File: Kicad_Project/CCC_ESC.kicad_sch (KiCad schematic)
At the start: 218 parts, among them J1 Conn_01x07, J2 Conn_01x06, J3 Conn_01x06, J4 Conn_01x06, SW1 Conn_01x02, U1 NCP5183 / TF2190-TAH, U2 NCP5183 / TF2190-TAH, U3 NCP5183 / TF2190-TAH, U4 NCS20034DR2G, U5 STM32F401CCU6_Balckpill, U6 PQDE6W-Q110 / RD5-110S12W, U7 TO220_replacement_module

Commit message: initial layout approach
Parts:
- QA1, QA2, QA3, QA4, QA5, QA6: footprint CCC_ESC_Custom_parts:TO220_horizontal_smallgate -> Package_DFN_QFN:DFNW-8_L8.3-W8.4-P2.00-BL
- TpGS1, TpGS2, TpGS3, TpGS4, TpGS5, TpGS6: footprint TestPoint:TestPoint_THTPad_D2.0mm_Drill1.0mm -> TestPoint:TestPoint_THTPad_D1.5mm_Drill0.7mm
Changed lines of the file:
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@@
       (effects (font (size 1.27 1.27)) (justify left) hide)
     )
-    (property "Footprint" "CCC_ESC_Custom_parts:TO220_horizontal_smallgate" (at 504.19 55.88 0)
+    (property "Footprint" "Package_DFN_QFN:DFNW-8_L8.3-W8.4-P2.00-BL" (at 504.19 55.88 0)
       (effects (font (size 1.27 1.27)) hide)
     )
@@
       (effects (font (size 1.27 1.27)) (justify left) hide)
     )
-    (property "Footprint" "CCC_ESC_Custom_parts:TO220_horizontal_smallgate" (at 474.98 55.88 0)
+    (property "Footprint" "Package_DFN_QFN:DFNW-8_L8.3-W8.4-P2.00-BL" (at 474.98 55.88 0)
       (effects (font (size 1.27 1.27)) hide)
     )
@@
       (effects (font (size 1.27 1.27)) (justify left) hide)
     )
-    (property "Footprint" "CCC_ESC_Custom_parts:TO220_horizontal_smallgate" (at 474.98 76.2 0)
+    (property "Footprint" "Package_DFN_QFN:DFNW-8_L8.3-W8.4-P2.00-BL" (at 474.98 76.2 0)
       (effects (font (size 1.27 1.27)) hide)
     )
@@
       (effects (font (size 1.27 1.27)) (justify left))
     )
-    (property "Footprint" "TestPoint:TestPoint_THTPad_D2.0mm_Drill1.0mm" (at 447.675 156.21 0)
+    (property "Footprint" "TestPoint:TestPoint_THTPad_D1.5mm_Drill0.7mm" (at 447.675 156.21 0)
       (effects (font (size 1.27 1.27)) hide)
     )
@@
       (effects (font (size 1.27 1.27)) (justify left))
     )
-    (property "Footprint" "TestPoint:TestPoint_THTPad_D2.0mm_Drill1.0mm" (at 445.77 95.25 0)
+    (property "Footprint" "TestPoint:TestPoint_THTPad_D1.5mm_Drill0.7mm" (at 445.77 95.25 0)
       (effects (font (size 1.27 1.27)) hide)
     )
@@
       (effects (font (size 1.27 1.27)) (justify right))
     )
-    (property "Footprint" "TestPoint:TestPoint_THTPad_D2.0mm_Drill1.0mm" (at 457.835 256.54 0)
+    (property "Footprint" "TestPoint:TestPoint_THTPad_D1.5mm_Drill0.7mm" (at 457.835 256.54 0)
       (effects (font (size 1.27 1.27)) hide)
     )
@@
       (effects (font (size 1.27 1.27)) (justify left) hide)
     )
-    (property "Footprint" "CCC_ESC_Custom_parts:TO220_horizontal_smallgate" (at 534.67 55.88 0)
+    (property "Footprint" "Package_DFN_QFN:DFNW-8_L8.3-W8.4-P2.00-BL" (at 534.67 55.88 0)
       (effects (font (size 1.27 1.27)) hide)
     )
@@
       (effects (font (size 1.27 1.27)) (justify left))
     )
-    (property "Footprint" "TestPoint:TestPoint_THTPad_D2.0mm_Drill1.0mm" (at 447.675 175.26 0)
+    (property "Footprint" "TestPoint:TestPoint_THTPad_D1.5mm_Drill0.7mm" (at 447.675 175.26 0)
       (effects (font (size 1.27 1.27)) hide)
     )
@@
       (effects (font (size 1.27 1.27)) (justify left) hide)
     )
-    (property "Footprint" "CCC_ESC_Custom_parts:TO220_horizontal_smallgate" (at 534.67 76.2 0)
+    (property "Footprint" "Package_DFN_QFN:DFNW-8_L8.3-W8.4-P2.00-BL" (at 534.67 76.2 0)
       (effects (font (size 1.27 1.27)) hide)
     )
@@
       (effects (font (size 1.27 1.27)) (justify left))
     )
-    (property "Footprint" "TestPoint:TestPoint_THTPad_D2.0mm_Drill1.0mm" (at 445.77 76.2 0)
+    (property "Footprint" "TestPoint:TestPoint_THTPad_D1.5mm_Drill0.7mm" (at 445.77 76.2 0)
       (effects (font (size 1.27 1.27)) hide)
     )
@@
       (effects (font (size 1.27 1.27)) (justify left) hide)
     )
-    (property "Footprint" "CCC_ESC_Custom_parts:TO220_horizontal_smallgate" (at 504.19 76.2 0)
+    (property "Footprint" "Package_DFN_QFN:DFNW-8_L8.3-W8.4-P2.00-BL" (at 504.19 76.2 0)
       (effects (font (size 1.27 1.27)) hide)
     )
@@
       (effects (font (size 1.27 1.27)) (justify left))
     )
-    (property "Footprint" "TestPoint:TestPoint_THTPad_D2.0mm_Drill1.0mm" (at 447.675 237.49 0)
+    (property "Footprint" "TestPoint:TestPoint_THTPad_D1.5mm_Drill0.7mm" (at 447.675 237.49 0)
       (effects (font (size 1.27 1.27)) hide)
     )

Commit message: initial layout approach
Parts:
- removed PH3, PH6, PH9: PhasePad, TestPoint:TestPoint_THTPad_D4.0mm_Drill2.0mm, symbol Connector:TestPoint
- removed TpVS1: TestPoint, TestPoint:TestPoint_THTPad_D2.0mm_Drill1.0mm, symbol Connector:TestPoint
- PHA_1: renamed from PH1; footprint TestPoint:TestPoint_THTPad_D4.0mm_Drill2.0mm -> TestPoint:my_2mm_slot
- PHA_2: renamed from PH2; footprint TestPoint:TestPoint_THTPad_D4.0mm_Drill2.0mm -> TestPoint:my_2mm_slot
- PHB_1: renamed from PH4; footprint TestPoint:TestPoint_THTPad_D4.0mm_Drill2.0mm -> TestPoint:my_2mm_slot
- PHB_2: renamed from PH5; footprint TestPoint:TestPoint_THTPad_D4.0mm_Drill2.0mm -> TestPoint:my_2mm_slot
- PHC_1: renamed from PH7; footprint TestPoint:TestPoint_THTPad_D4.0mm_Drill2.0mm -> TestPoint:my_2mm_slot
- PHC_2: renamed from PH8; footprint TestPoint:TestPoint_THTPad_D4.0mm_Drill2.0mm -> TestPoint:my_2mm_slot
- QA1, QA2, QA3, QA4, QA5, QA6: value CRST030N10N -> NVMTSC4D3N15MC
- QB1, QB2, QB3, QB4, QB5, QB6, QC1, QC2, QC3, QC4, QC5, QC6: value CRST030N10N -> NVMTSC4D3N15MC; footprint CCC_ESC_Custom_parts:TO220_horizontal_smallgate -> Package_DFN_QFN:DFNW-8_L8.3-W8.4-P2.00-BL
- TpGS1, TpGS2: footprint TestPoint:TestPoint_THTPad_D1.5mm_Drill0.7mm -> TestPoint:TestPoint_THTPad_D4.0mm_Drill2.0mm
- renumbered CX11 to CD1, CX12 to CD2, CX13 to CD3, CX14 to CD4, CX15 to CD5, CX16 to CD6, R43 to RG1, R46 to RG10, R58 to RG11, R66 to RG12, R53 to RG13, R59 to RG14, R63 to RG15, R54 to RG16, R60 to RG17, R64 to RG18, R55 to RG2, R61 to RG3, R44 to RG4, R56 to RG5, R62 to RG6, R45 to RG7, R57 to RG8, R65 to RG9
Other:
- moved on the sheet: CD1, CD2, CD3, CD4, CD5, CD6, CX1, CX17, CX18, CX19, CX2, CX20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

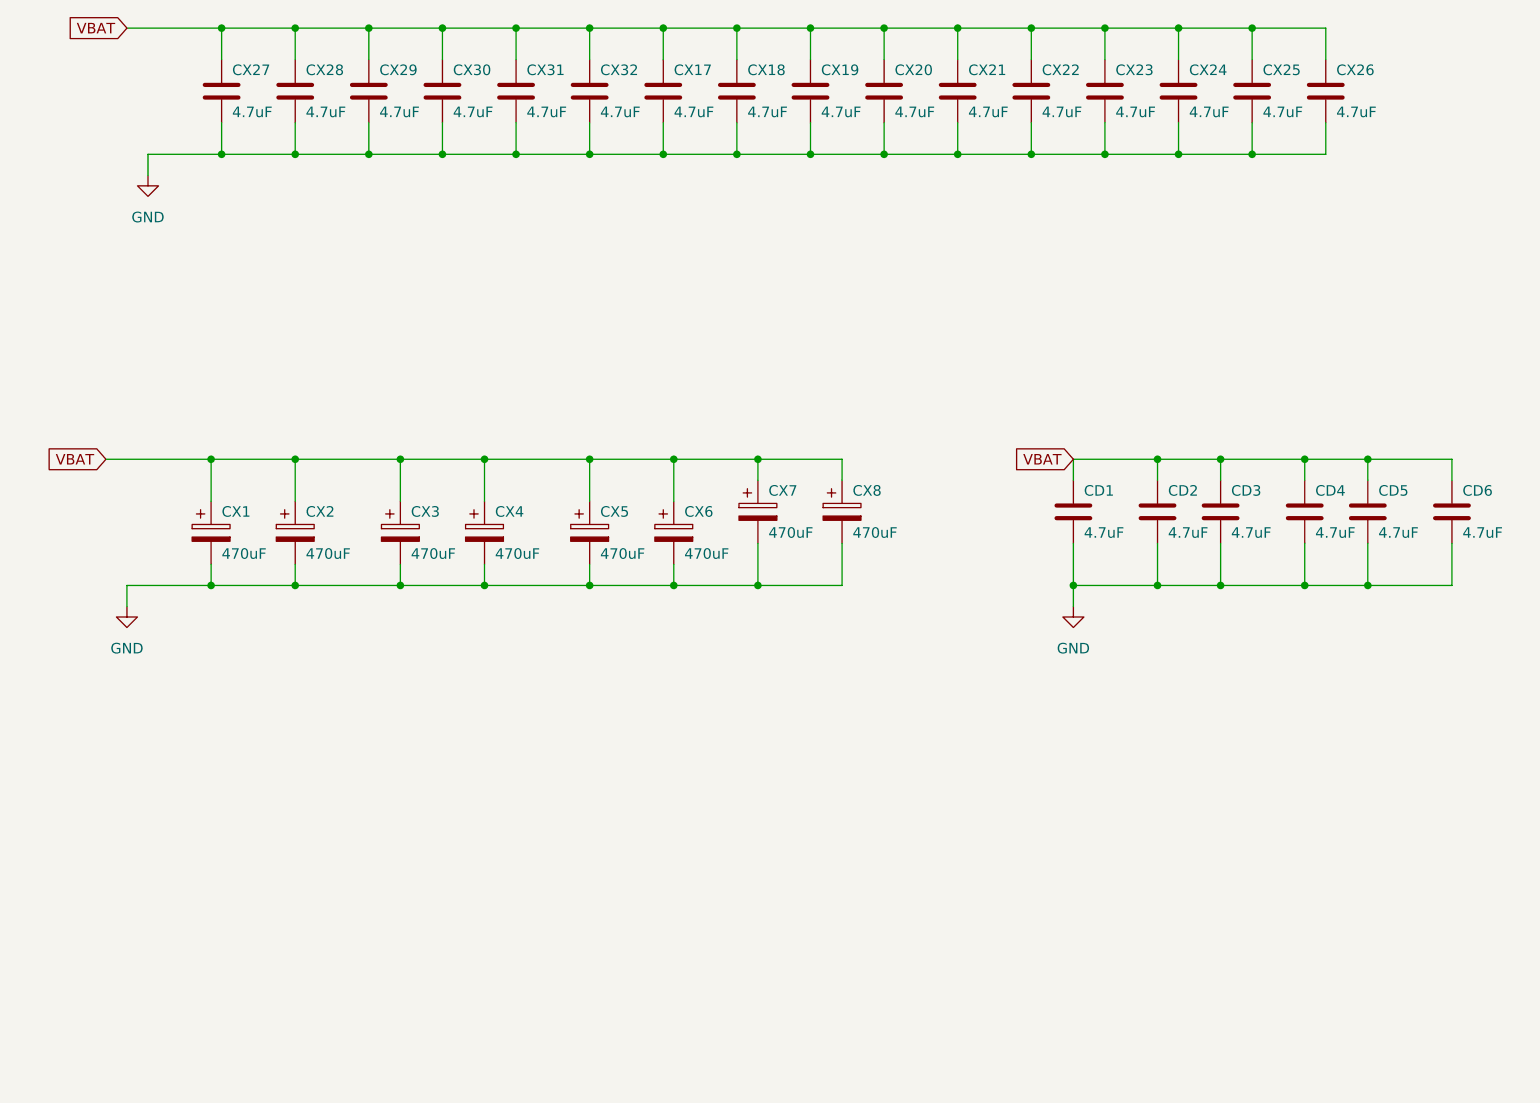
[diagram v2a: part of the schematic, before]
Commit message: reversed side of bus bars
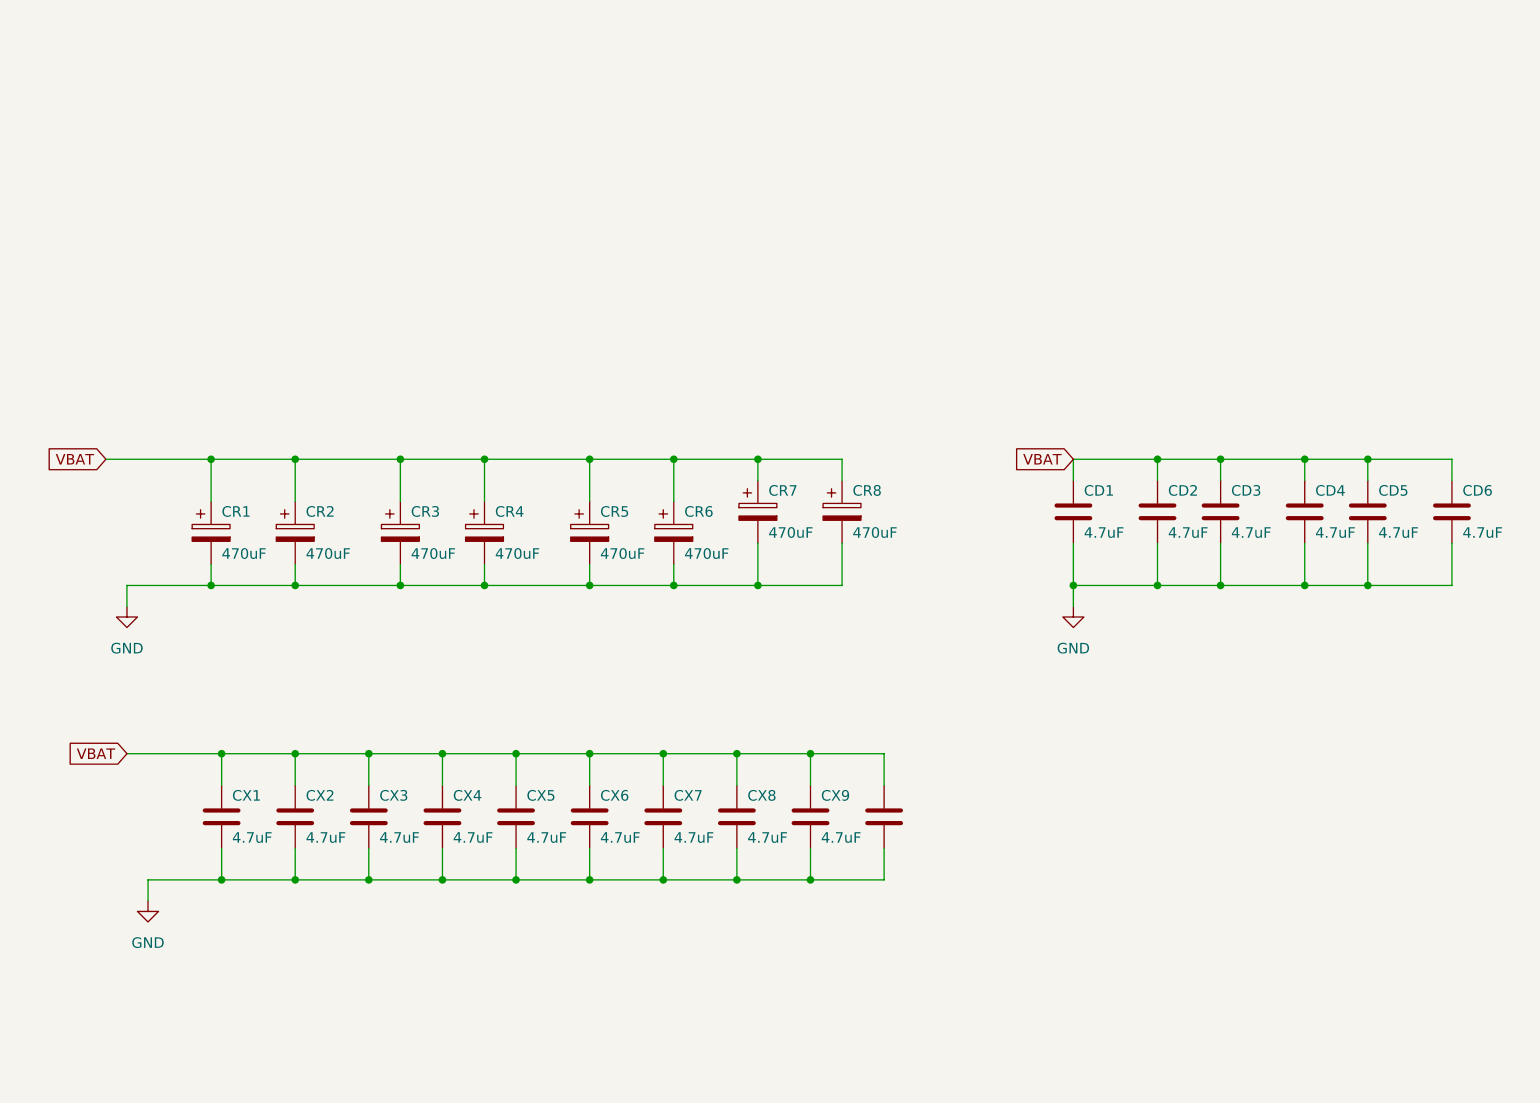
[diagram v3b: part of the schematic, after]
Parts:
- removed CX21, CX22, CX23, CX24, CX25, CX26: 4.7uF, Capacitor_SMD:C_1210_3225Metric, symbol Device:C
- renumbered CX1 to CR1, CX2 to CR2, CX3 to CR3, CX4 to CR4, CX5 to CR5, CX6 to CR6, CX7 to CR7, CX8 to CR8, CX27 to CX1, CX28 to CX2, CX29 to CX3, CX30 to CX4, CX31 to CX5, CX32 to CX6, CX17 to CX7, CX18 to CX8, CX19 to CX9
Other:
- moved on the sheet: CX1, CX2, CX3, CX4, CX5, CX6, CX7, CX8, CX9

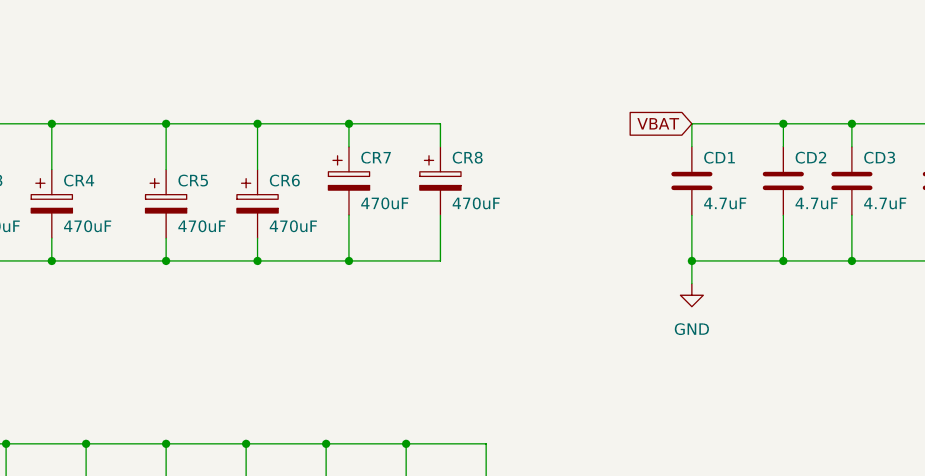
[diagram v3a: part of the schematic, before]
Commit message: reversed side of bus bars
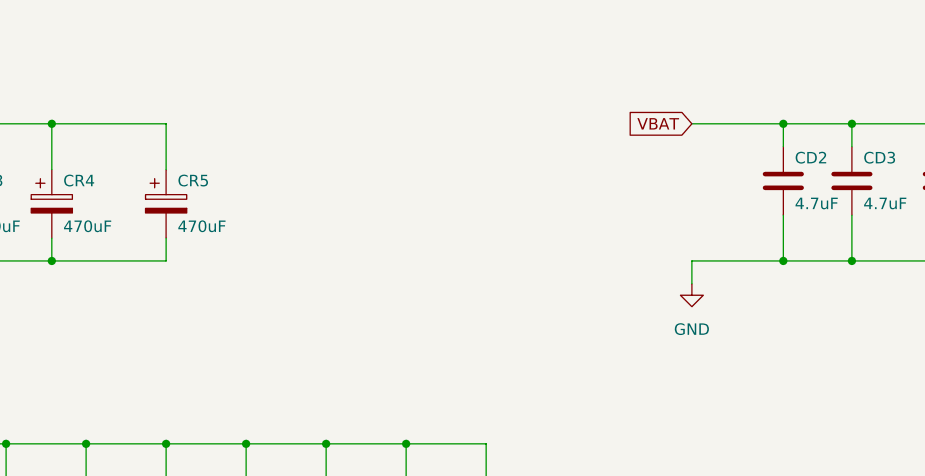
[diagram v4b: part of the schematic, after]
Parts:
- removed CD1: 4.7uF, Capacitor_SMD:C_1210_3225Metric, symbol Device:C
- removed CR6, CR7, CR8: 470uF, CCC_ESC_Custom_parts:CAP_Polaryzed, symbol Device:C_Polarized
- CR1, CR2, CR3, CR4, CR5: footprint CCC_ESC_Custom_parts:CAP_Polaryzed -> Capacitor_THT:CP_Radial_D18.0mm_P7.50mm

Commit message: added in resistors, gate/source caps
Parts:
- added CSG1, CSG2, CSG3, CSG4, CSG5, CSG6: C, Capacitor_SMD:C_0805_2012Metric, symbol Device:C
- added R42, R43: R470, Resistor_SMD:R_0603_1608Metric, symbol Device:R
- added RN7: 470R, Resistor_SMD:R_Array_Concave_4x0603, symbol Device:R_Pack04
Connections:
- net AL_GATESIG: now also CSG2.1
- net AU_GATESIG: now also CSG1.1
- net BL_GATESIG: now also CSG4.1
- net BU_GATESIG: now also CSG3.1
- net CL_GATESIG: now also CSG6.1
- net CU_GATESIG: now also CSG5.1
- net HIN_A: now also RN7.8 (R1.2); no longer U5.25 (PA8)
- net HIN_B: now also RN7.6 (R3.2); no longer U5.26 (PA9)
- net HIN_C: now also R43.1; no longer U5.27 (PA10)
- net LIN_A: now also RN7.7 (R2.2); no longer U5.22 (PB13)
- net LIN_B: now also RN7.5 (R4.2); no longer U5.23 (PB14)
- net LIN_C: now also R42.1; no longer U5.24 (PB15)
- net PHASE_A: now also CSG1.2
- net PHASE_B: now also CSG3.2
- net PHASE_C: now also CSG5.2
- net at NT5.1, QC2.3, QC4.3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: now also CSG6.2
- net at NT1.1, QA2.3, QA4.3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: now also CSG2.2
- net at NT3.1, QB2.3, QB4.3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: now also CSG4.2
- new net _HIN_A: RN7.1 (R1.1), U5.25 (PA8)
- new net _HIN_B: RN7.3 (R3.1), U5.26 (PA9)
- new net _HIN_C: R43.2, U5.27 (PA10)
- new net _LIN_A: RN7.2 (R2.1), U5.22 (PB13)
- new net _LIN_B: RN7.4 (R4.1), U5.23 (PB14)
- new net _LIN_C: R42.2, U5.24 (PB15)
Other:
- moved on the sheet: CD2, CD3, CD4, CD5, CD6, R37, R39, R48, R50, R52

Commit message: first draft
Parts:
- removed CSG1, CSG2, CSG3, CSG4, CSG5, CSG6: C, Capacitor_SMD:C_0805_2012Metric, symbol Device:C
- added CGS1, CGS2, CGS3, CGS4, CGS5, CGS6, CGS7, CGS8, CGS9: 6pF, Capacitor_SMD:C_0603_1608Metric, symbol Device:C
- added CGS10, CGS11, CGS12, CGS13, CGS14, CGS15, CGS16, CGS17, CGS18: 6pF, Capacitor_SMD:C_0603_1608Metric, symbol Device:C_Small
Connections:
- net PHASE_A: now also CGS1.1, CGS2.1, CGS3.1
- net PHASE_B: now also CGS4.1, CGS5.1, CGS6.1
- net PHASE_C: now also CGS7.1, CGS8.1, CGS9.1
- net at NT5.1, QC2.3, QC4.3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: now also CGS16.2, CGS17.2, CGS18.2
- net at QA3.1, RG2.1: now also CGS2.2
- net at QC2.1, RG16.1: now also CGS16.1
- net at QA1.1, RG1.1: now also CGS1.2
- net at QB5.1, RG9.1: now also CGS6.2
- net at QB1.1, RG7.1: now also CGS4.2
- net at QA2.1, RG4.1: now also CGS10.1
- net at NT1.1, QA2.3, QA4.3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: now also CGS10.2, CGS11.2, CGS12.2
- net at NT3.1, QB2.3, QB4.3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: now also CGS13.2, CGS14.2, CGS15.2
- net at QB4.1, RG11.1: now also CGS14.1
- net at QB6.1, RG12.1: now also CGS15.1
- net at QB3.1, RG8.1: now also CGS5.2
- net at QA5.1, RG3.1: now also CGS3.2
- net at QC6.1, RG18.1: now also CGS18.1
- net at QC1.1, RG13.1: now also CGS7.2
- net at QC5.1, RG15.1: now also CGS9.2
- net at QC3.1, RG14.1: now also CGS8.2
- net at QC4.1, RG17.1: now also CGS17.1
- net at QA4.1, RG5.1: now also CGS11.1
- net at QB2.1: now also RG10.2, CGS13.1; no longer RG10.1
- net at QA6.1, RG6.1: now also CGS12.1
- net BL_GATESIG: no longer names the net of R50.2, RG11.2, RG12.2, TpGS4.1, U2.4 (DRVL)
- net BL_GATESIG: now also RG10.1; no longer RG10.2
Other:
- moved on the sheet: RG10, RG12, RG9

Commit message: first draft
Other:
- note added: "Note: several test points were removed in order to add additional components."
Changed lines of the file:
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@@
     (effects (font (size 1.27 1.27)) (justify left bottom))
+  )
+  (text "Note: several test points were removed in order to add additional components."
+    (at 354.33 132.08 0)
+    (effects (font (size 4 4)) (justify left bottom))
   )
   (text "Phase sensing" (at 312.42 154.94 0)
